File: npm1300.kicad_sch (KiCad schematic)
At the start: 19 parts, among them U2 nPM1300-QEXX

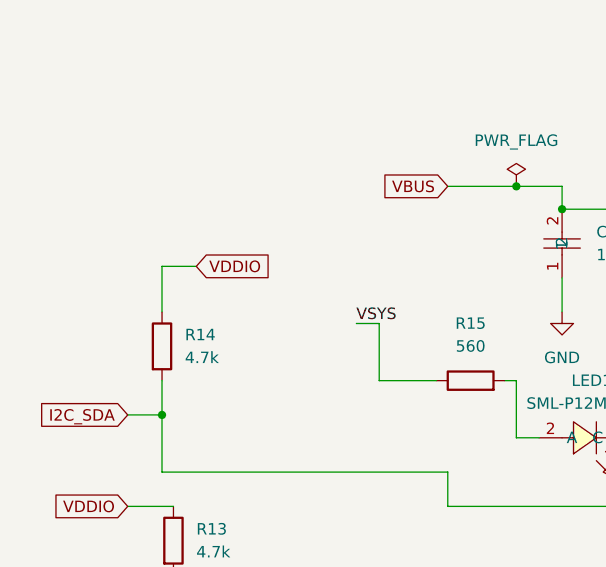
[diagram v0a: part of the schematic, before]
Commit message: Update soil moisture PCB layout and npm1300 VDDIO routing.
Co-authored-by: Cursor <cursoragent@cursor.com>
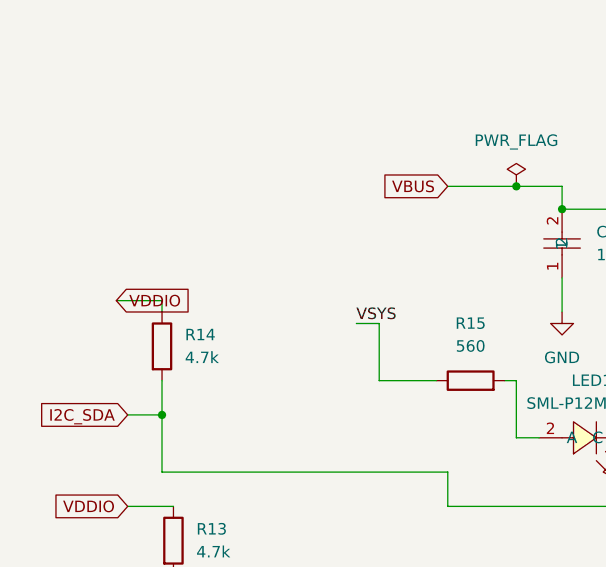
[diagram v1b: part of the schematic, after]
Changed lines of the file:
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@@
 	(wire
 		(pts
-			(xy 35.56 73.66) (xy 35.56 68.58)
+			(xy 35.56 73.66) (xy 35.56 72.39)
 		)
 		(stroke
@@
 	(wire
 		(pts
-			(xy 35.56 68.58) (xy 39.37 68.58)
+			(xy 35.56 72.39) (xy 30.48 72.39)
 		)
 		(stroke
@@
 	(global_label "VDDIO"
 		(shape input)
-		(at 39.37 68.58 0)
+		(at 30.48 72.39 0)
 		(fields_autoplaced yes)
 		(effects
@@
 		)
 		(property "Intersheetrefs" "${INTERSHEET_REFS}"
-			(at 47.9191 68.58 0)
+			(at 39.0291 72.39 0)
 			(hide yes)
 			(show_name no)

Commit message: Update soil moisture PCB and npm1300 VDDIO routing; add espc6_ph and first layout projects.
Co-authored-by: Cursor <cursoragent@cursor.com>
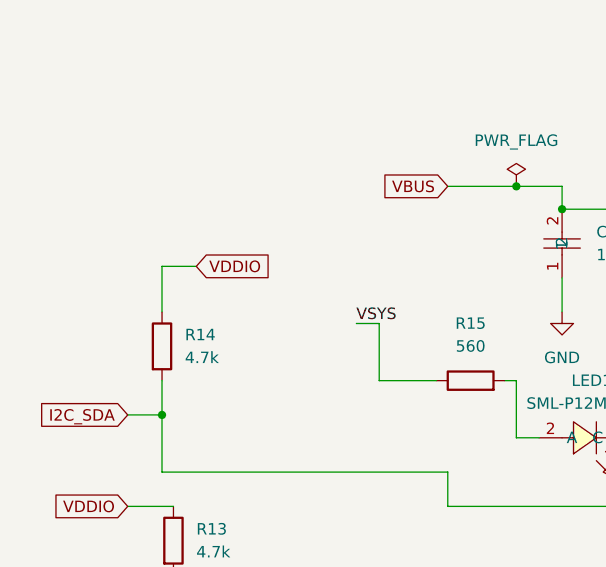
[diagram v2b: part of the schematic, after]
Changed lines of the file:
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@@
 	(wire
 		(pts
-			(xy 35.56 73.66) (xy 35.56 72.39)
+			(xy 35.56 73.66) (xy 35.56 68.58)
 		)
 		(stroke
@@
 	(wire
 		(pts
-			(xy 35.56 72.39) (xy 30.48 72.39)
+			(xy 35.56 68.58) (xy 39.37 68.58)
 		)
 		(stroke
@@
 	(global_label "VDDIO"
 		(shape input)
-		(at 30.48 72.39 0)
+		(at 39.37 68.58 0)
 		(fields_autoplaced yes)
 		(effects
@@
 		)
 		(property "Intersheetrefs" "${INTERSHEET_REFS}"
-			(at 39.0291 72.39 0)
+			(at 47.9191 68.58 0)
 			(hide yes)
 			(show_name no)
